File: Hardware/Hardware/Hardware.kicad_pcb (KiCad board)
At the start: 2 copper layers, 30 parts, among them Q1 MMUN2112LT1G, SW1 Button, U1 AZ1117CH-3.3TRG1, U2 USBLC6-2SC6, U3 STM32F303CCT6, U4 BMA253, Y1 8Mhz 10pf

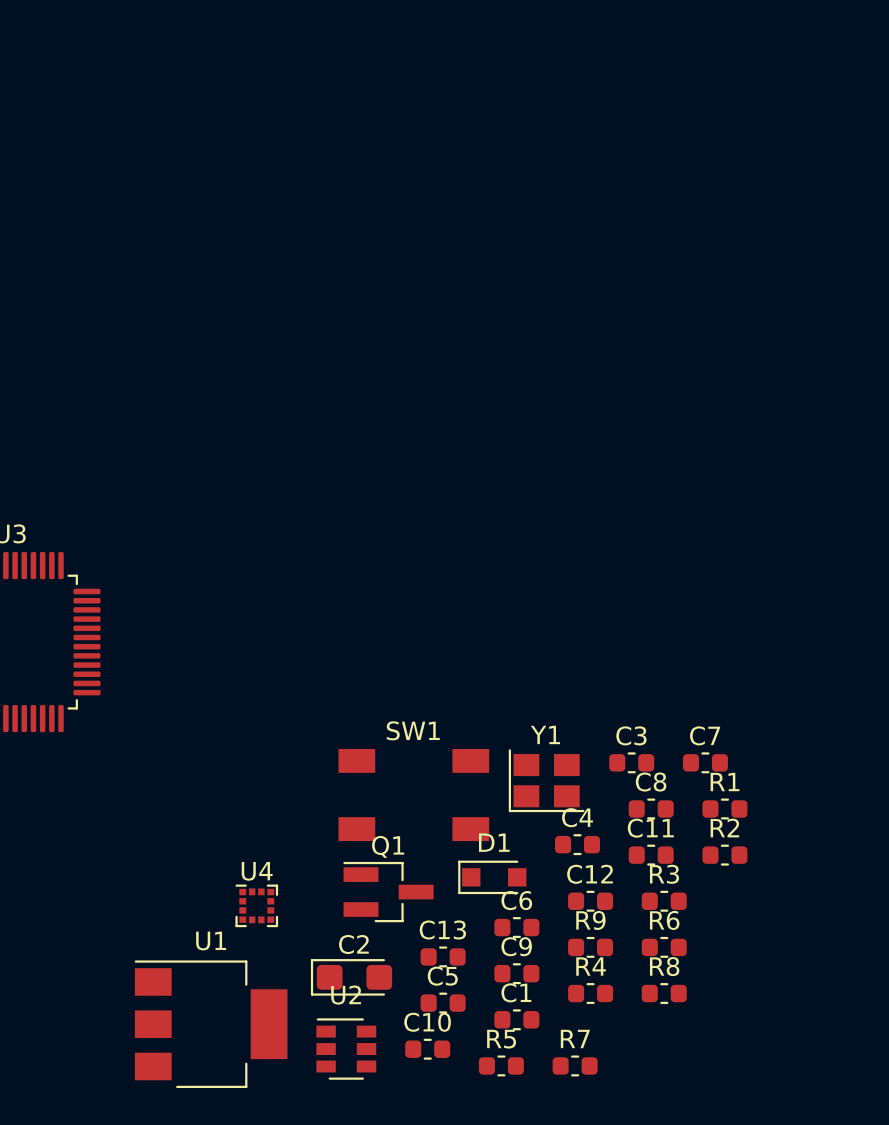
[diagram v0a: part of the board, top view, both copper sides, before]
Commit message: update Schematic make everything looks nice
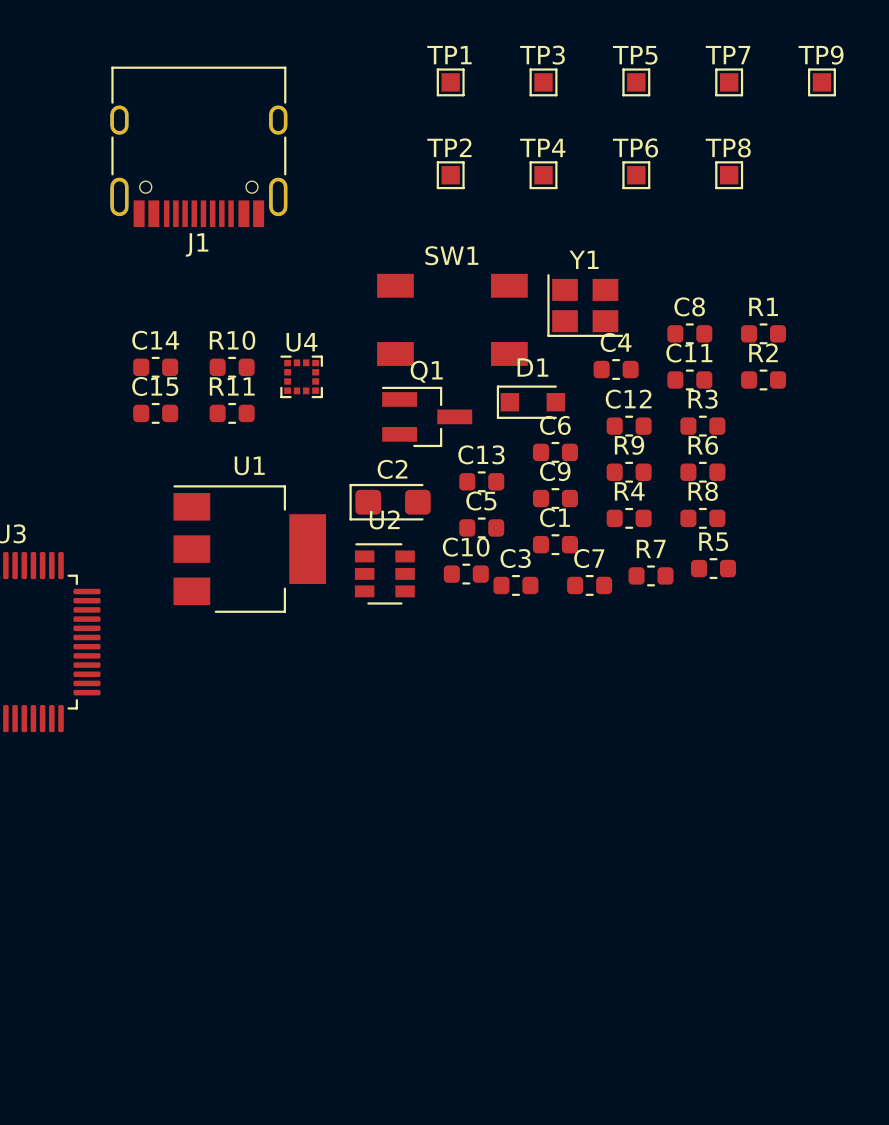
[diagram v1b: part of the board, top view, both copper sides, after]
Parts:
- added C14: 100nF, Capacitor_SMD:C_0603_1608Metric, F.Cu at (113.8, 61.4)
- added C15: 100nF, Capacitor_SMD:C_0603_1608Metric, F.Cu at (113.8, 63.9)
- added J1: TYPE-C-31-M-12, Connector_USB:USB_C_Receptacle_HRO_TYPE-C-31-M-12, F.Cu at (116.1, 49.0)
- added R10: R_Small, Resistor_SMD:R_0603_1608Metric, F.Cu at (117.9, 61.4)
- added R11: R_Small, Resistor_SMD:R_0603_1608Metric, F.Cu at (117.9, 63.9)
- added TP1: TestPoint, TestPoint:TestPoint_Pad_1.0x1.0mm, F.Cu at (129.8, 45.9)
- added TP2: TestPoint, TestPoint:TestPoint_Pad_1.0x1.0mm, F.Cu at (129.8, 51.0)
- added TP3: TestPoint, TestPoint:TestPoint_Pad_1.0x1.0mm, F.Cu at (134.8, 45.9)
- added TP4: TestPoint, TestPoint:TestPoint_Pad_1.0x1.0mm, F.Cu at (134.8, 51.0)
- added TP5: TestPoint, TestPoint:TestPoint_Pad_1.0x1.0mm, F.Cu at (139.9, 45.9)
- added TP6: TestPoint, TestPoint:TestPoint_Pad_1.0x1.0mm, F.Cu at (139.9, 51.0)
- added TP7: TestPoint, TestPoint:TestPoint_Pad_1.0x1.0mm, F.Cu at (144.9, 45.9)
- added TP8: TestPoint, TestPoint:TestPoint_Pad_1.0x1.0mm, F.Cu at (144.9, 51.0)
- added TP9: TestPoint, TestPoint:TestPoint_Pad_1.0x1.0mm, F.Cu at (150.0, 45.9)
- D1: value D -> 1N4148WS
- moved R5 29.4 mm to (144.1, 72.3)
- moved U4 28.9 mm to (121.7, 61.9)
- moved R7 27.0 mm to (140.7, 72.8)
- moved C13 25.9 mm to (131.5, 67.6)
- moved D1 25.9 mm to (134.3, 63.3)
- moved R3 25.9 mm to (143.5, 64.6)
- moved C1 25.9 mm to (135.5, 71.0)
- moved C12 25.9 mm to (139.5, 64.6)
- moved C2 25.9 mm to (126.7, 68.7)
- moved C4 25.9 mm to (138.8, 61.5)
- moved C8 25.9 mm to (142.8, 59.6)
- moved Q1 25.9 mm to (128.5, 64.1)
- moved R1 25.9 mm to (146.8, 59.6)
- moved C5 25.9 mm to (131.5, 70.1)
- moved R6 25.9 mm to (143.5, 67.1)
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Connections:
- net /MCU/D+ renamed Net-(R8-Pad2)
- net /MCU/D- renamed Net-(R6-Pad2)
- R2 pad 1: (no net) -> /MCU/CC1
- R3 pad 1: (no net) -> /MCU/CC2
- U3 pad 37: (no net) -> /SDA
- U3 pad 38: (no net) -> /SCL
- U4 pad 1: (no net) -> GND
- U4 pad 12: (no net) -> /SCL
- U4 pad 2: (no net) -> /SDA
- U4 pad 4: (no net) -> GND

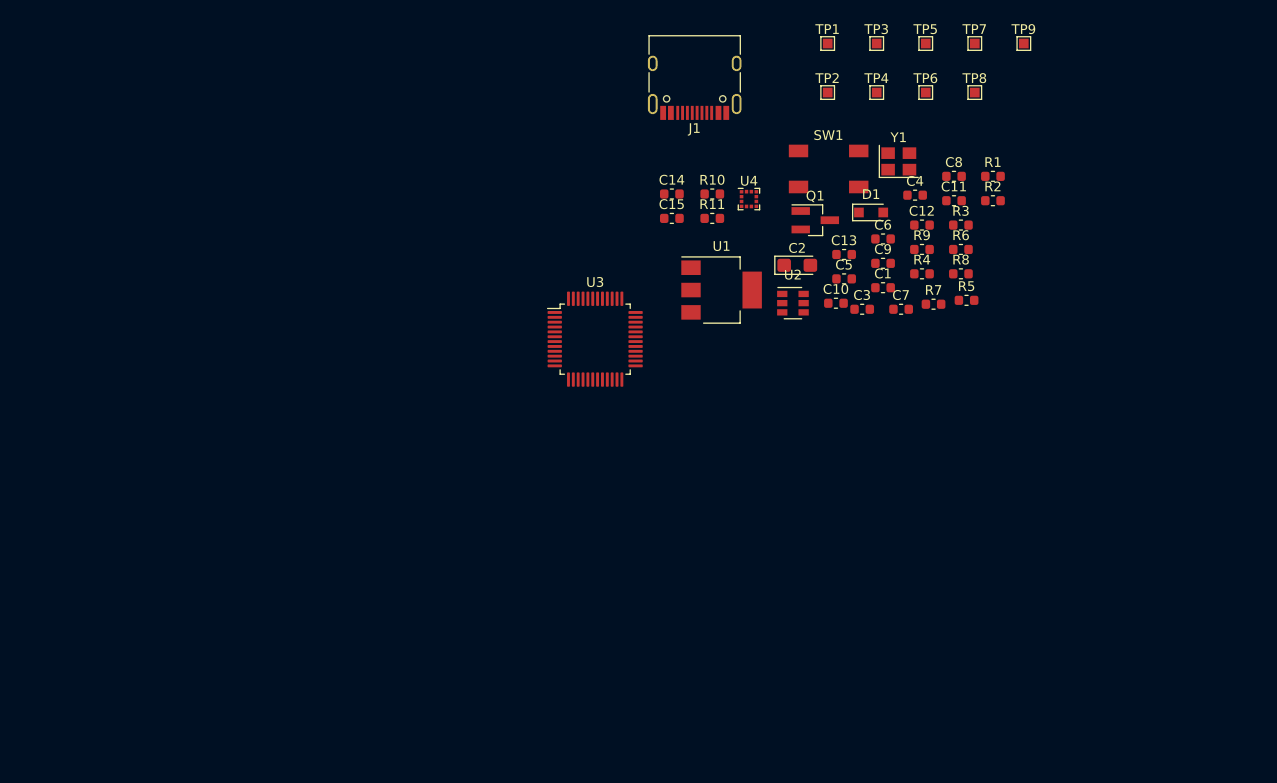
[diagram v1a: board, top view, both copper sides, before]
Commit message: fix some mistake on wiring, use ListBox instead of menubutton
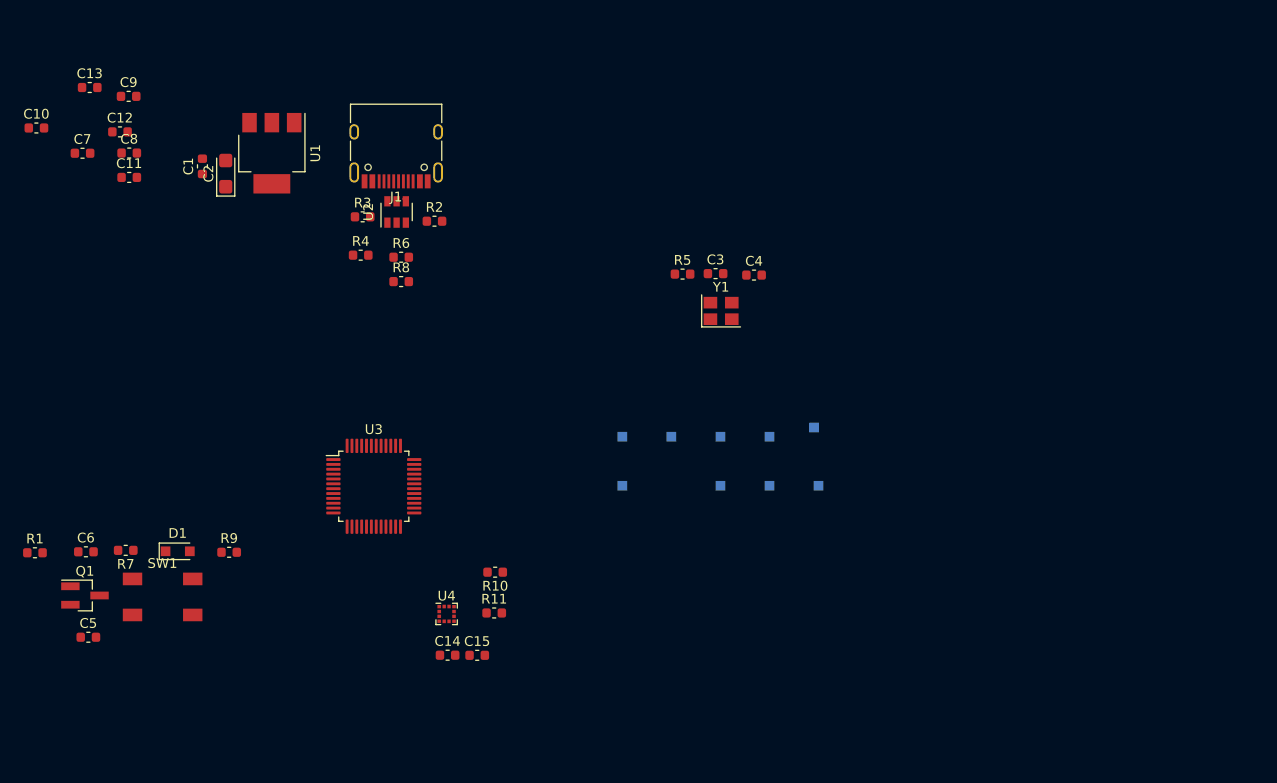
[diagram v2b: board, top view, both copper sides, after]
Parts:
- TP1, TP2, TP3, TP4, TP5, TP6, TP7, TP8, TP9: moved to B.Cu
- moved R1 106.0 mm to (48.1, 98.3)
- moved C6 88.2 mm to (53.4, 98.2)
- moved R7 87.0 mm to (57.5, 98.1), turned to 180 degrees
- moved C5 86.1 mm to (53.6, 107.0)
- moved C7 85.8 mm to (53.0, 57.2)
- moved C11 85.0 mm to (57.9, 59.7)
- moved C8 85.0 mm to (57.9, 57.2)
- moved Q1 84.6 mm to (53.3, 102.8)
- moved C10 84.3 mm to (48.3, 54.6)
- moved C12 83.2 mm to (56.9, 55.0)
- moved SW1 81.5 mm to (61.3, 102.9)
- moved C13 79.6 mm to (53.8, 50.4)
- moved C9 79.6 mm to (57.8, 51.3)
- moved D1 79.5 mm to (62.9, 98.2)
- moved R9 77.9 mm to (68.2, 98.3)
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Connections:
- net Net-(R6-Pad2) renamed /MCU/D-
- net Net-(R8-Pad2) renamed /MCU/D+

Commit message: say goodbye to the L3GD220 and LSM303. They are obsolete parts no one cares about.
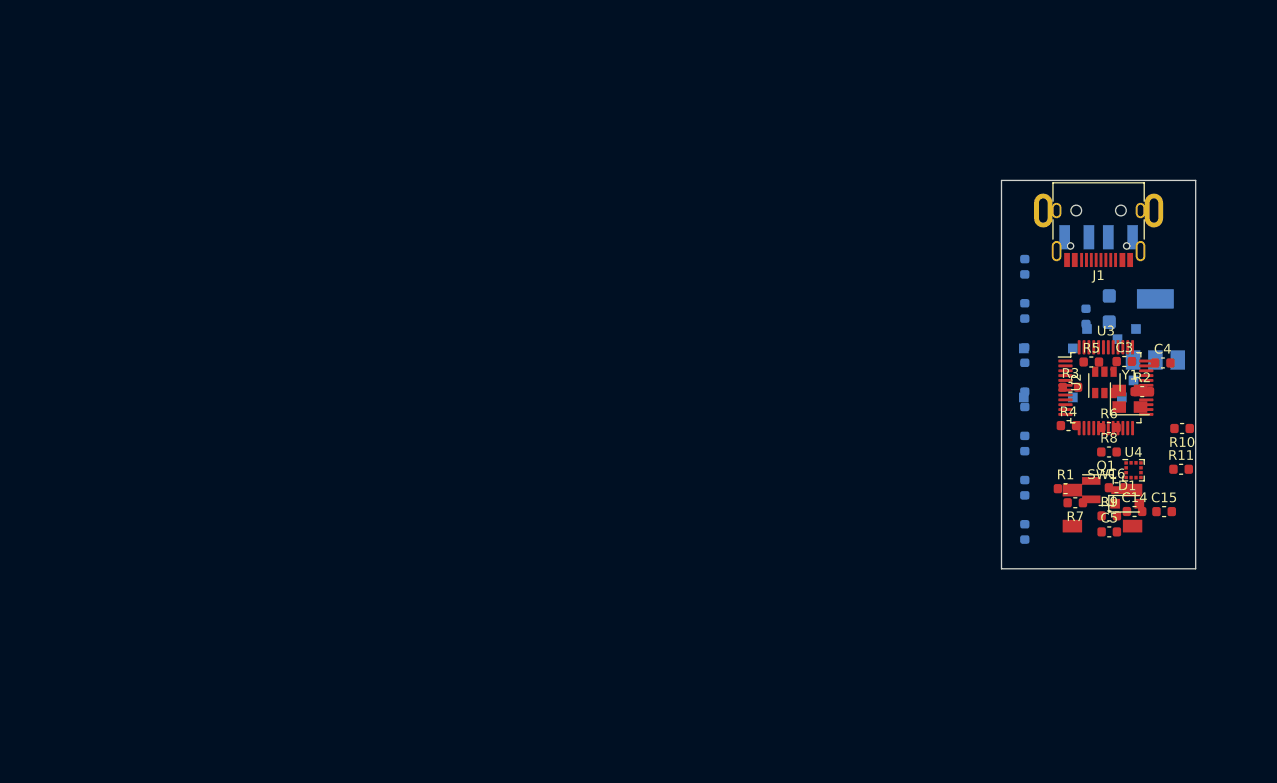
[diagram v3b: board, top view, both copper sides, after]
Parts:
- added J2: USB_A, Connector_USB:USB_A_CNCTech_1001-011-01101_Horizontal, B.Cu at (157.7, 56.2)
- C1, C10, C11, C12, C13, C2, C7, C8, C9, U1: moved to B.Cu
- R10, R11: value R_Small -> 1.5k
- R2, R3: value 56K -> 56k
- R4, R5: value 1.5K -> 1.5k
- moved C10 110.0 mm to (150.1, 96.2), turned to 90 degrees
- moved C6 106.4 mm to (159.6, 91.7)
- moved R1 106.4 mm to (154.3, 91.8)
- moved C5 105.7 mm to (158.8, 96.2)
- moved Q1 105.7 mm to (158.4, 91.9)
- moved C13 103.1 mm to (150.1, 87.1), turned to 90 degrees
- moved C7 103.0 mm to (150.1, 91.6), turned to 90 degrees
- moved D1 97.9 mm to (160.7, 93.3)
- moved R7 97.9 mm to (155.3, 93.2)
- moved SW1 97.2 mm to (158.1, 93.8)
- moved C12 97.2 mm to (150.1, 82.5), turned to 90 degrees
- moved C9 96.1 mm to (150.1, 78.0), turned to 90 degrees
- moved C11 93.3 mm to (150.1, 73.4), turned to 90 degrees
- moved C8 93.0 mm to (150.1, 68.9), turned to 90 degrees
- moved U1 92.8 mm to (163.6, 75.3), turned to 90 degrees
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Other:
- board outline added: 20 x 40 mm

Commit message: tiny improvement
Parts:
- removed J2: USB_A, Connector_USB:USB_A_CNCTech_1001-011-01101_Horizontal
- removed SW1: Button, KiCad:K2-1187SQ-A4SW-06
- added JP1: Jumper_NO_Small, Connector_PinSocket_2.54mm:PinSocket_1x02_P2.54mm_Vertical, F.Cu at (136.7, 90.7)
- C14, C15, U4: moved to B.Cu
- R6, R8: footprint Resistor_SMD:R_0603_1608Metric -> Resistor_SMD:R_0402_1005Metric
- moved TP1 37.5 mm to (126.3, 67.3)
- moved TP4 36.8 mm to (127.1, 62.5)
- moved TP2 36.0 mm to (122.6, 63.2)
- moved TP3 31.8 mm to (129.1, 67.4)
- moved TP9 30.6 mm to (130.4, 75.2)
- moved Q1 27.6 mm to (132.1, 100.1)
- moved TP7 27.0 mm to (130.7, 70.6)
- moved TP8 26.0 mm to (131.4, 66.3)
- moved D1 23.2 mm to (138.6, 100.3)
- moved C5 21.1 mm to (137.8, 97.8)
- moved TP6 20.8 mm to (133.3, 89.7)
- moved TP5 20.6 mm to (132.3, 92.9)
- moved C6 18.5 mm to (141.1, 90.2)
- moved R2 17.9 mm to (150.4, 68.3)
- moved R9 17.4 mm to (141.8, 98.3)
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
